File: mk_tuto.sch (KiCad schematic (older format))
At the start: 14 parts

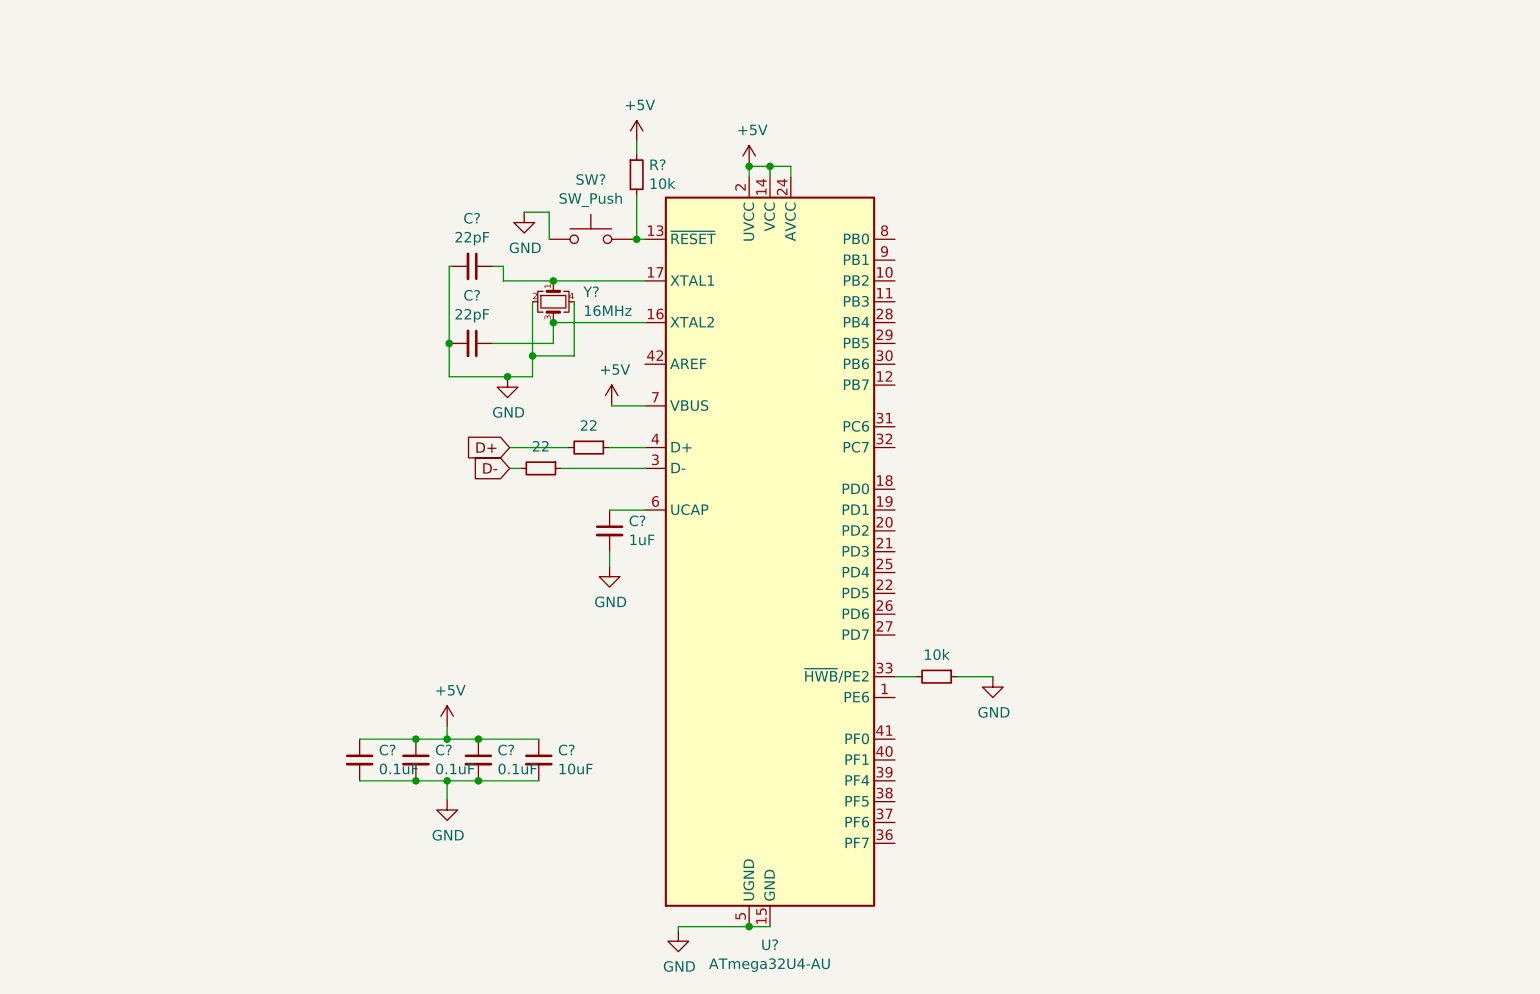
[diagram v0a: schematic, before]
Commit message: Assigned PCB parts to the symbols
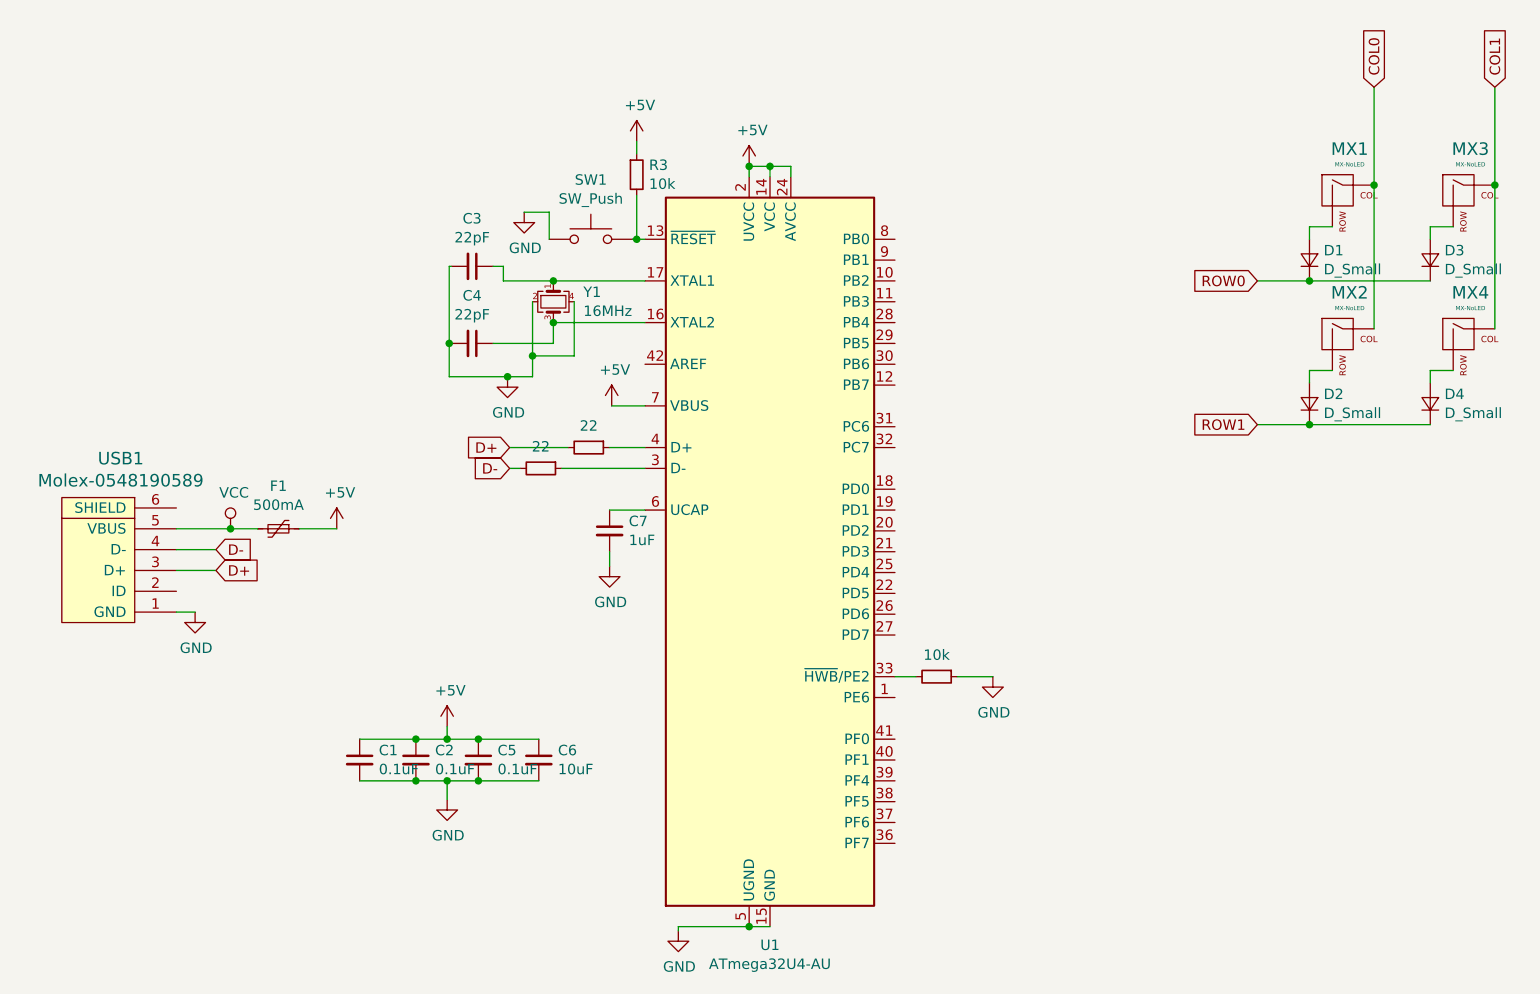
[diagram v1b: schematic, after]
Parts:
- added D1, D2, D3, D4: D_Small, Diode_SMD:D_SOD-123, symbol Device:D_Small
- added F1: 500mA, Fuse:Fuse_1206_3216Metric, symbol Device:Polyfuse_Small
- added MX1, MX2, MX3, MX4: MX-NoLED, MX_Alps_Hybrid:MX-1.5U-NoLED, symbol MX_Alps_Hybrid:MX-NoLED
- added USB1: Molex-0548190589, random-keyboard-parts:Molex-0548190589, symbol random-keyboard-parts:Molex-0548190589
- C1, C2, C3, C4, C5, C6, C7: renamed from C?; footprint (none) -> Capacitor_SMD:C_0805_2012Metric
- R1, R2, R3, R4: renamed from R?; footprint (none) -> Resistor_SMD:R_0805_2012Metric
- SW1: renamed from SW?; footprint (none) -> random-keyboard-parts:SKQG-1155865
- Y1: renamed from Y?; footprint (none) -> Crystal:Crystal_SMD_3225-4Pin_3.2x2.5mm
- gave numbers to parts that had none: 1
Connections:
- net +5V: now also F1.1
- net D+: now also USB1.3 (D+)
- net D-: now also USB1.4 (D-)
- net GND: now also USB1.1 (GND)
- new net: D3.2 (A), MX3.2 (ROW)
- new net: D1.2 (A), MX1.2 (ROW)
- new net: D2.2 (A), MX2.2 (ROW)
- new net: D4.2 (A), MX4.2 (ROW)
- new net COL0: MX1.1 (COL), MX2.1 (COL)
- new net COL1: MX3.1 (COL), MX4.1 (COL)
- new net ROW0: D1.1 (K), D3.1 (K)
- new net ROW1: D2.1 (K), D4.1 (K)
- new net VCC: F1.2, USB1.5 (VBUS)

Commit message: Finished the PCB routing, will have to redo it cleanly
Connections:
- net COL0: now also U1.28 (PB4)
- net COL1: now also U1.29 (PB5)
- net ROW0: now also U1.27 (PD7)
- net ROW1: now also U1.30 (PB6)
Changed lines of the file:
@@
 EESchema Schematic File Version 4
+LIBS:mk_tuto-cache
 EELAYER 30 0
 EELAYER END
@@
 Wire Wire Line
 	9280 1310 9280 1780
+Text GLabel 6480 2440 2    50   Input ~ 0
+COL0
+Text GLabel 6480 2540 2    50   Input ~ 0
+COL1
+Text GLabel 6460 3940 2    50   Input ~ 0
+ROW0
+Text GLabel 6480 2640 2    50   Input ~ 0
+ROW1
+Wire Wire Line
+	6400 3940 6460 3940
+Wire Wire Line
+	6480 2640 6400 2640
+Wire Wire Line
+	6400 2540 6480 2540
+Wire Wire Line
+	6480 2440 6400 2440
 $EndSCHEMATC
